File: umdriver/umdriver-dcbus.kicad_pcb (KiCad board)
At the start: 2 copper layers, 95 x 100 mm, 0 parts

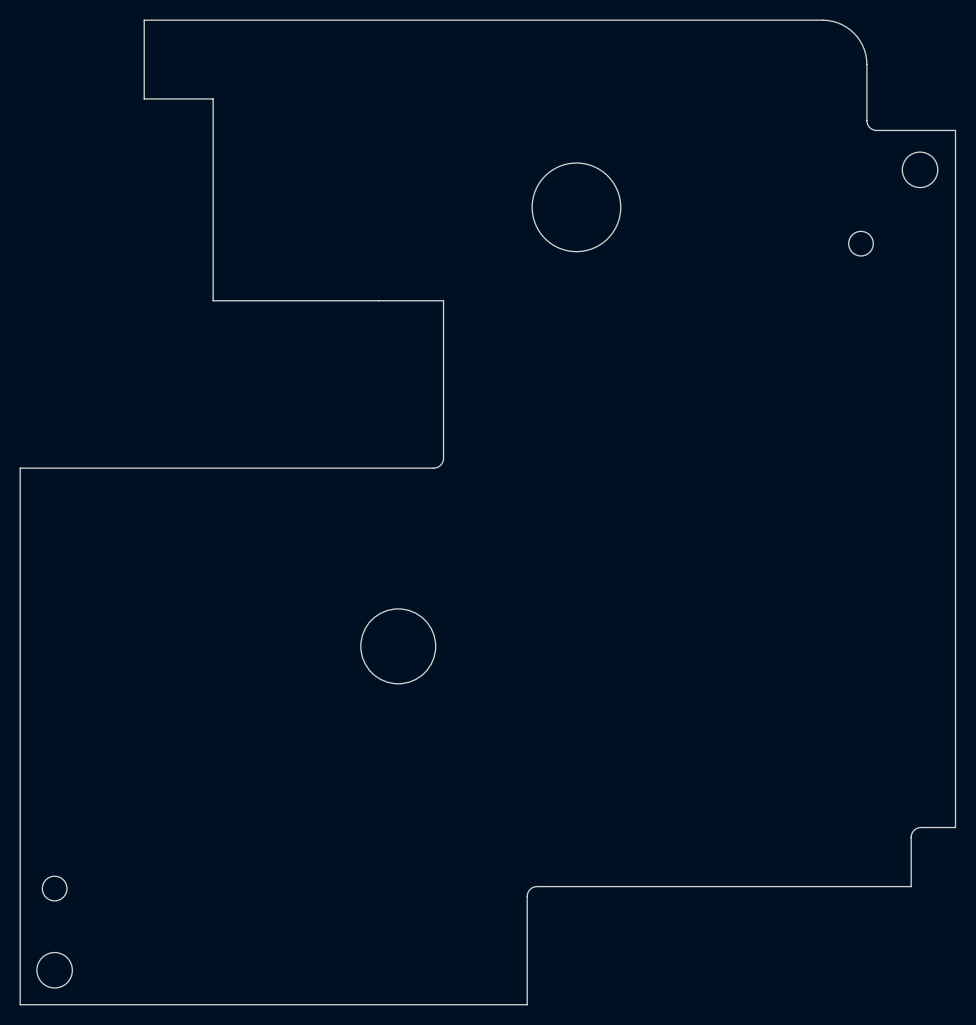
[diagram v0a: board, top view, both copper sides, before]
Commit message: Main board routing complete
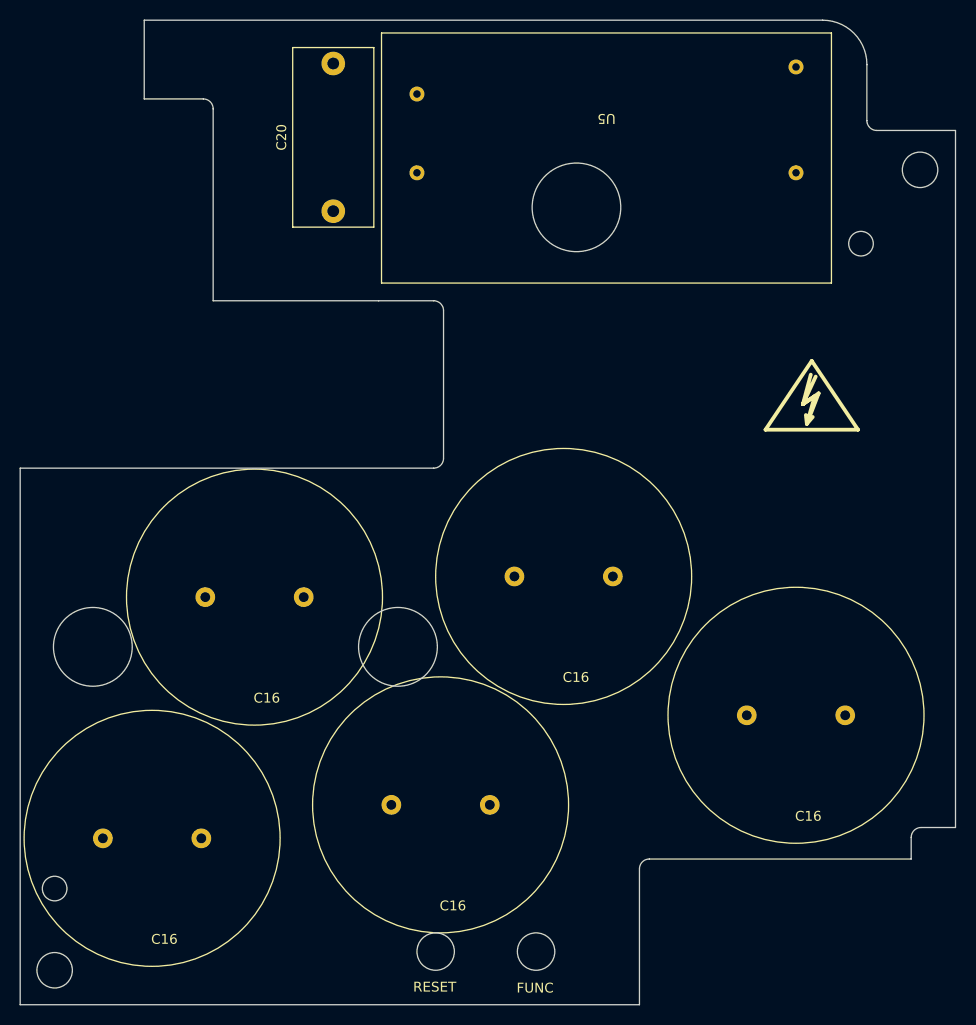
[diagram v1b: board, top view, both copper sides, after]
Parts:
- added C16: >9000, Capacitor_THT:C_Radial_D18.0mm_H35.5mm_P7.50mm, F.Cu at (151.9, 108.5)
- added C16: >9000, Capacitor_THT:C_Radial_D18.0mm_H35.5mm_P7.50mm, F.Cu at (110.1, 135.1)
- added C16: >9000, Capacitor_THT:C_Radial_D18.0mm_H35.5mm_P7.50mm, F.Cu at (139.4, 131.7)
- added C16: >9000, Capacitor_THT:C_Radial_D18.0mm_H35.5mm_P7.50mm, F.Cu at (175.5, 122.6)
- added C16: >9000, Capacitor_THT:C_Radial_D18.0mm_H35.5mm_P7.50mm, F.Cu at (120.5, 110.6)
- added C20: C, Capacitor_THT:C_Rect_L18.0mm_W8.0mm_P15.00mm_FKS3_FKP3, F.Cu at (123.5, 71.4)
- added SYM1: SYM_Flash_Small, umdriver:Symbol_HighVoltage_Type2_Silkscreen_VerySmall, F.Cu at (172.1, 90.8)
- added U5: PSU, umdriver:IRM-10-15, F.Cu at (170.5, 67.5)
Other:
- outline, holes or cut-outs redrawn
- board text added: "FUNC"
- board text added: "RESET"
